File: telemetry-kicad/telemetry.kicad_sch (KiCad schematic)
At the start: 0 parts

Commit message: Changed MCU to LQFP64 footprint, added TVS and reverse polarity protection, added buck converter chip.
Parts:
- added C1, C2, C3, C4, C5, C6: 1uF, symbol Device:C
- added C10, C11: 1uF, Capacitor_SMD:C_0402_1005Metric_Pad0.74x0.62mm_HandSolder, symbol Device:C
- added C7, C8: 10uF, symbol Device:C
- added C9: 10uF, Capacitor_SMD:C_0402_1005Metric_Pad0.74x0.62mm_HandSolder, symbol Device:C
- added D1: BZT52-C15S-AU_R1_000A1, symbol Device:D_Zener
- added D2: D20V0L1B2LP-7B, symbol Device:D_TVS
- added F1: 100mA Polyfuse, Capacitor_SMD:C_0603_1608Metric_Pad1.08x0.95mm_HandSolder, symbol Device:Polyfuse
- added Q1: DMP3099LQ-7, Package_TO_SOT_SMD:SOT-23, symbol Transistor_FET:DMP3099L
- added R1: 10k, symbol Device:R_US
- added R2: 10K, symbol Device:R_US
- added SW1: SW_NRST, symbol Switch:SW_Push
- added SW2: SW_BOOT0, symbol Switch:SW_Push
- added U1: STM32H523RCT7, LQFP64_STM, symbol telemetry:STM32H523RCT7
- added U2: AP2112K-3.3, Package_TO_SOT_SMD:SOT-23-5, symbol Regulator_Linear:AP2112K-3.3
- added U3: LMR33630ADDA, Package_SO:Texas_HSOP-8-1EP_3.9x4.9mm_P1.27mm_ThermalVias, symbol Regulator_Switching:LMR33630ADDA
- added U4: ASM330LHHXG1TR, LGA14_2P5X3_STM, symbol telemetry:ASM330LHHXG1TR
- added U5: TCAN1044VDRQ1, D0008A-IPC_A, symbol telemetry:TCAN1044VDRQ1
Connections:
- new net: R1.1, SW2.1, U1.60 (BOOT0)
- new net: C1.1, C2.1, C3.1, C4.1, C6.1, C7.1, C8.1
- new net: SW1.1, U1.7 (NRST)
- new net: U3.1 (GND), U3.9 (GND)
- new net: D1.1 (K), Q1.2 (S)
- new net: D1.2 (A), Q1.1 (G), R2.1
- new net +3.3V: C5.1, SW2.2, U1.1 (VBAT), U1.13 (VDDA), U1.19 (VDD), U1.32 (VDD), U1.48 (VDD), U1.64 (VDD)
- new net +3V3: C11.1, U2.5 (VOUT)
- new net Earth: C1.2, C2.2, C3.2, C4.2, C5.2, C6.2, C7.2, C8.2, D2.2 (A2), R1.2, R2.2, SW1.2, U1.12 (VSSA), U1.18 (VSS), U1.31 (VSS), U1.47 (VSS), U1.63 (VSS)
- new net GND: C10.2, C11.2, C9.1, U2.2 (GND)
- new net VBUS: F1.1
- new net VIN: D2.1 (A1), Q1.3 (D)
- new net VIN_LDO: C10.1, C9.2, F1.2, U2.1 (VIN), U2.3 (EN)
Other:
- note added: "Linear Voltage Regulator"
- note added: "Reverse Polarity Protection and TVS"

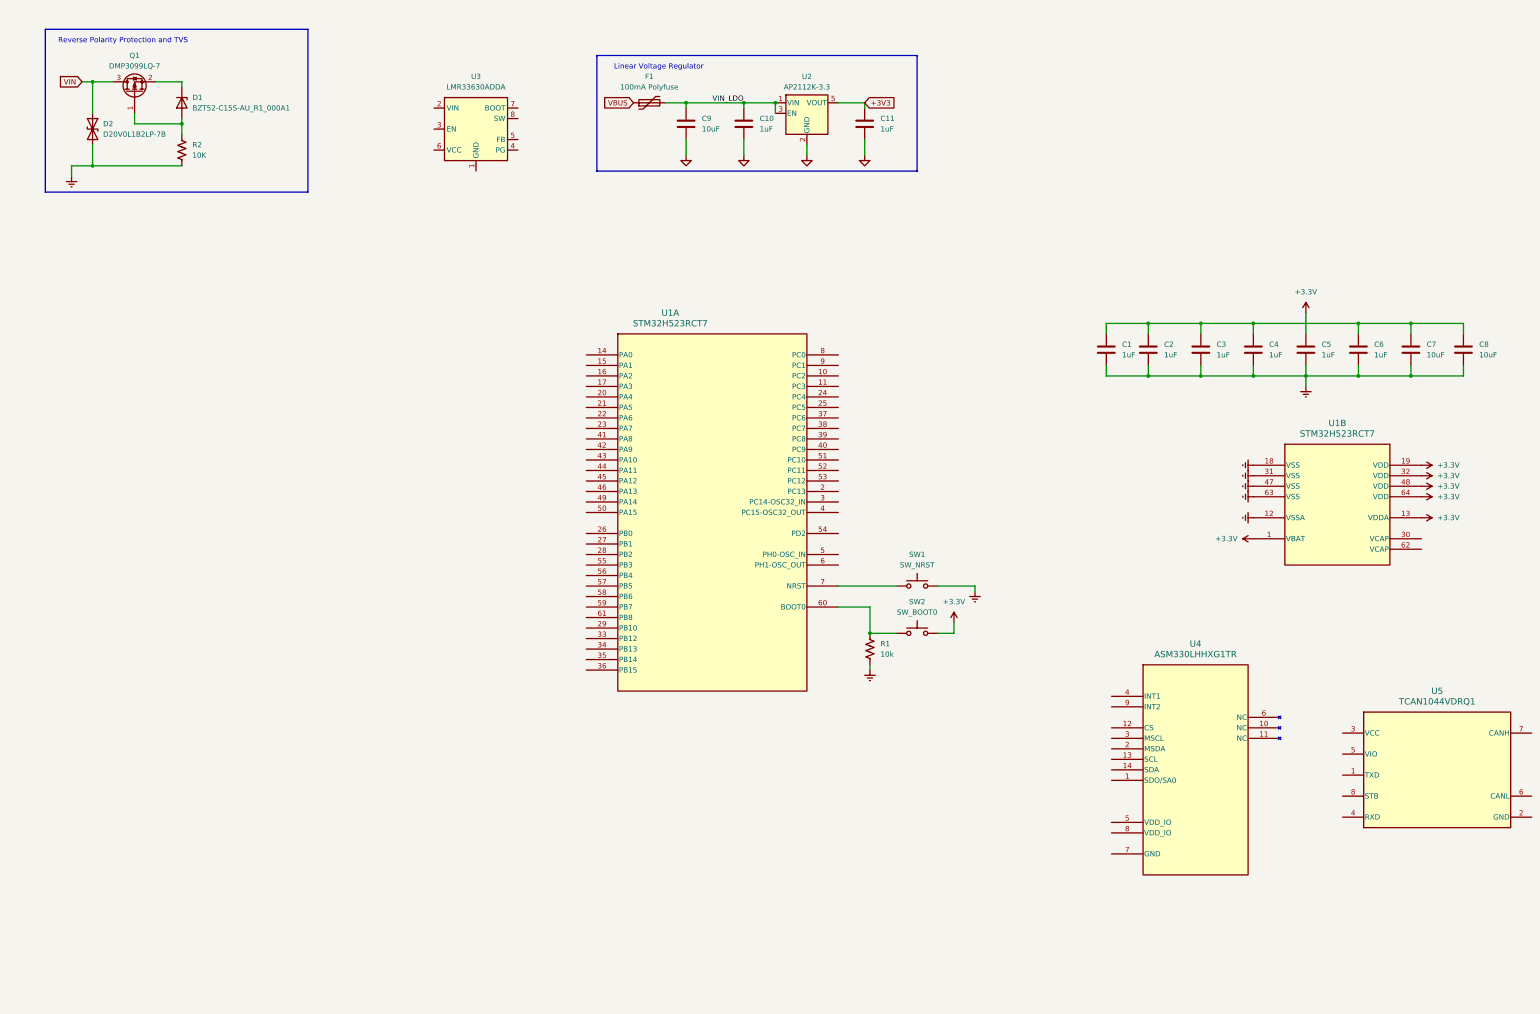
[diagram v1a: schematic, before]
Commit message: Developed schematic with all components, need to check Ublox integration and STM32 USB debugging and impliment SWD.
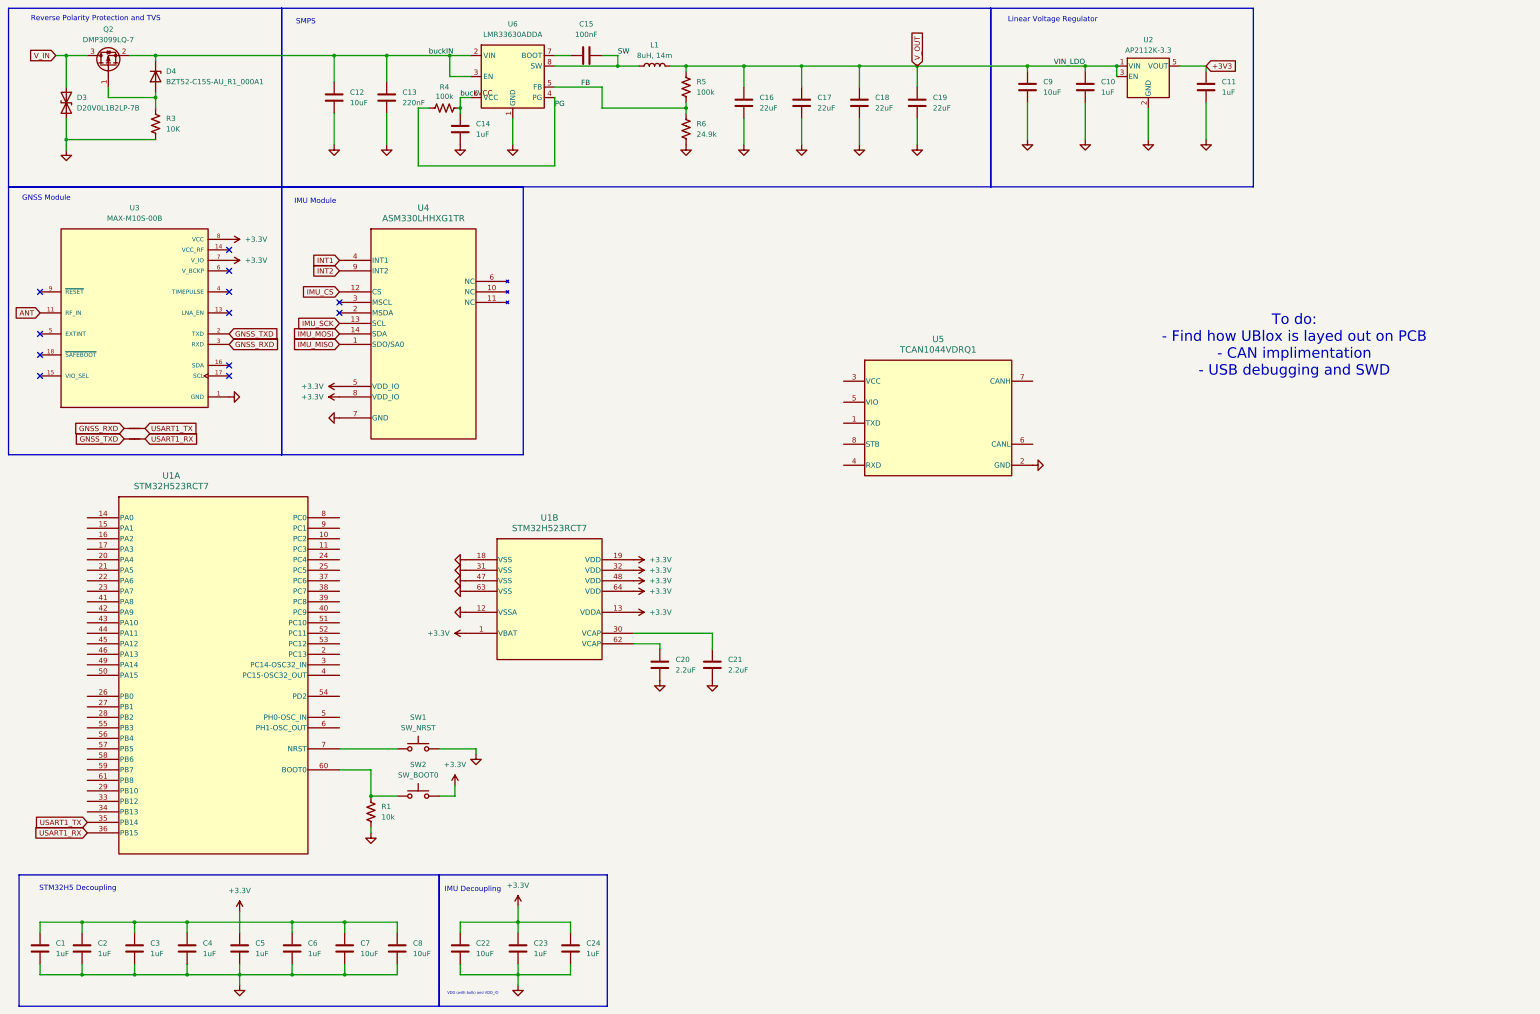
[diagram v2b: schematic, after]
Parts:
- removed D1: BZT52-C15S-AU_R1_000A1, symbol Device:D_Zener
- removed D2: D20V0L1B2LP-7B, symbol Device:D_TVS
- removed F1: 100mA Polyfuse, Capacitor_SMD:C_0603_1608Metric_Pad1.08x0.95mm_HandSolder, symbol Device:Polyfuse
- removed Q1: DMP3099LQ-7, Package_TO_SOT_SMD:SOT-23, symbol Transistor_FET:DMP3099L
- removed R2: 10K, symbol Device:R_US
- removed U3: LMR33630ADDA, Package_SO:Texas_HSOP-8-1EP_3.9x4.9mm_P1.27mm_ThermalVias, symbol Regulator_Switching:LMR33630ADDA
- added C12: 10uF, Capacitor_SMD:C_0805_2012Metric_Pad1.18x1.45mm_HandSolder, symbol Device:C
- added C13: 220nF, Capacitor_SMD:C_0805_2012Metric_Pad1.18x1.45mm_HandSolder, symbol Device:C
- added C14: 1uF, Capacitor_SMD:C_0805_2012Metric_Pad1.18x1.45mm_HandSolder, symbol Device:C
- added C15: 100nF, Capacitor_SMD:C_0805_2012Metric_Pad1.18x1.45mm_HandSolder, symbol Device:C
- added C16, C17, C18, C19: 22uF, Capacitor_SMD:C_0805_2012Metric_Pad1.18x1.45mm_HandSolder, symbol Device:C
- added C20, C21: 2.2uF, symbol Device:C
- added C22: 10uF, Capacitor_SMD:C_0402_1005Metric_Pad0.74x0.62mm_HandSolder, symbol Device:C
- added C23, C24: 1uF, Capacitor_SMD:C_0402_1005Metric_Pad0.74x0.62mm_HandSolder, symbol Device:C
- added D3: D20V0L1B2LP-7B, Capacitor_SMD:C_0402_1005Metric_Pad0.74x0.62mm_HandSolder, symbol Device:D_TVS
- added D4: BZT52-C15S-AU_R1_000A1, Diode_SMD:D_SOD-123, symbol Device:D_Zener
- added L1: 8uH, 14m, Inductor_SMD:L_TaiTech_TMPC1265_13.5x12.5mm, symbol Device:L
- added NT1, NT2: NetTie_2, symbol Device:NetTie_2
- added Q2: DMP3099LQ-7, Package_TO_SOT_SMD:SOT-23, symbol Transistor_FET:DMP3099L
- added R3: 10K, Capacitor_SMD:C_0805_2012Metric_Pad1.18x1.45mm_HandSolder, symbol Device:R_US
- added R4, R5: 100k, Capacitor_SMD:C_0805_2012Metric_Pad1.18x1.45mm_HandSolder, symbol Device:R_US
- added R6: 24.9k, Capacitor_SMD:C_0805_2012Metric_Pad1.18x1.45mm_HandSolder, symbol Device:R_US
- added U3: MAX-M10S-00B, MAX-M10S-00B, symbol telemetry:MAX-M10S-00B
- added U6: LMR33630ADDA, Package_SO:Texas_HSOP-8-1EP_3.9x4.9mm_P1.27mm_ThermalVias, symbol Regulator_Switching:LMR33630ADDA
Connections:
- net Earth is gone; now on net GND: C1.2, C2.2, C3.2, C4.2, C5.2, C6.2, C7.2, C8.2, R1.2, SW1.2, U1.12 (VSSA), U1.18 (VSS), U1.31 (VSS), U1.47 (VSS), U1.63 (VSS)
- net +3.3V: now also U4.5 (VDD_IO), U4.8 (VDD_IO), C22.2, C23.1, C24.1, U3.7 (V_IO), U3.8 (VCC)
- net GND: now also U4.7 (GND), U5.2 (GND), C12.2, C13.2, C14.2, C16.2, C17.2, C18.2, C19.2, C20.2, C21.2, C22.1, C23.2, C24.2, D3.2 (A2), R3.2, R6.2, U3.1 (GND), U3.10 (GND), U3.12 (GND), U6.1 (GND), U6.9 (GND)
- net IMU_MISO: now reaches U4.1 (SDO/SA0)
- net IMU_CS: now reaches U4.12 (CS)
- net IMU_SCK: now reaches U4.13 (SCL)
- net IMU_MOSI: now reaches U4.14 (SDA)
- net INT1: now reaches U4.4 (INT1)
- net INT2: now reaches U4.9 (INT2)
- net at U1.30 (VCAP): now also C21.1
- net at U1.62 (VCAP): now also C20.1
- net USART1_TX: now reaches U1.35 (PB14)
- net USART1_TX: now also NT2.1
- net USART1_RX: now reaches U1.36 (PB15)
- net USART1_RX: now also NT1.1
- net VIN_LDO renamed V_OUT
- net V_OUT: now also C16.1, C17.1, C18.1, C19.1, L1.2, R5.1
- new net: D4.2 (A), Q2.1 (G), R3.1
- new net: C15.1, U6.7 (BOOT)
- new net ANT: U3.11 (RF_IN)
- new net FB: R5.2, R6.1, U6.5 (FB)
- new net GNSS_RXD: NT2.2, U3.3 (RXD)
- new net GNSS_TXD: NT1.2, U3.2 (TXD)
- new net PG: R4.1, U6.4 (PG)
- new net SW: C15.2, L1.1, U6.8 (SW)
- new net V_IN: D3.1 (A1), Q2.3 (D)
- new net buckIN: C12.1, C13.1, D4.1 (K), Q2.2 (S), U6.2 (VIN), U6.3 (EN)
- new net buckVCC: C14.1, R4.2, U6.6 (VCC)
- no-connect marks 0 -> 12
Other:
- note added: "GNSS Module"
- note added: "IMU Decoupling"
- note added: "IMU Module"
- note added: "SMPS"
- note added: "STM32H5 Decoupling"
- note added: "To do: - Find how UBlox is layed out on PCB - CAN implimentation - USB debugging and SWD"
- note added: "VDD (with bulk) and VDD_IO"
- moved on the sheet: C1, C10, C11, C2, C3, C4, C5, C6, C7, C8, C9, R1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

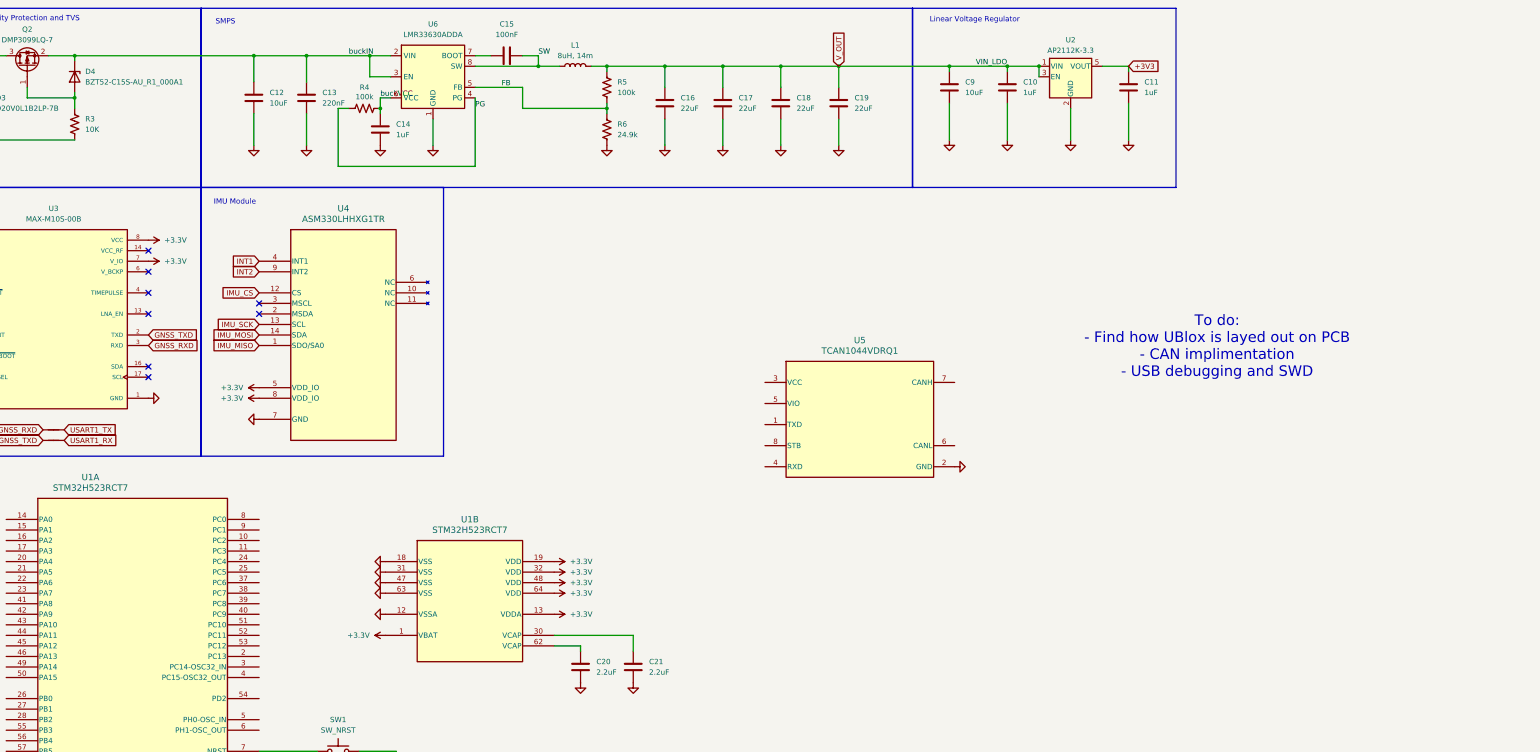
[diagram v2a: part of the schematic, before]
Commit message: Added power mux between USB and 12V car power
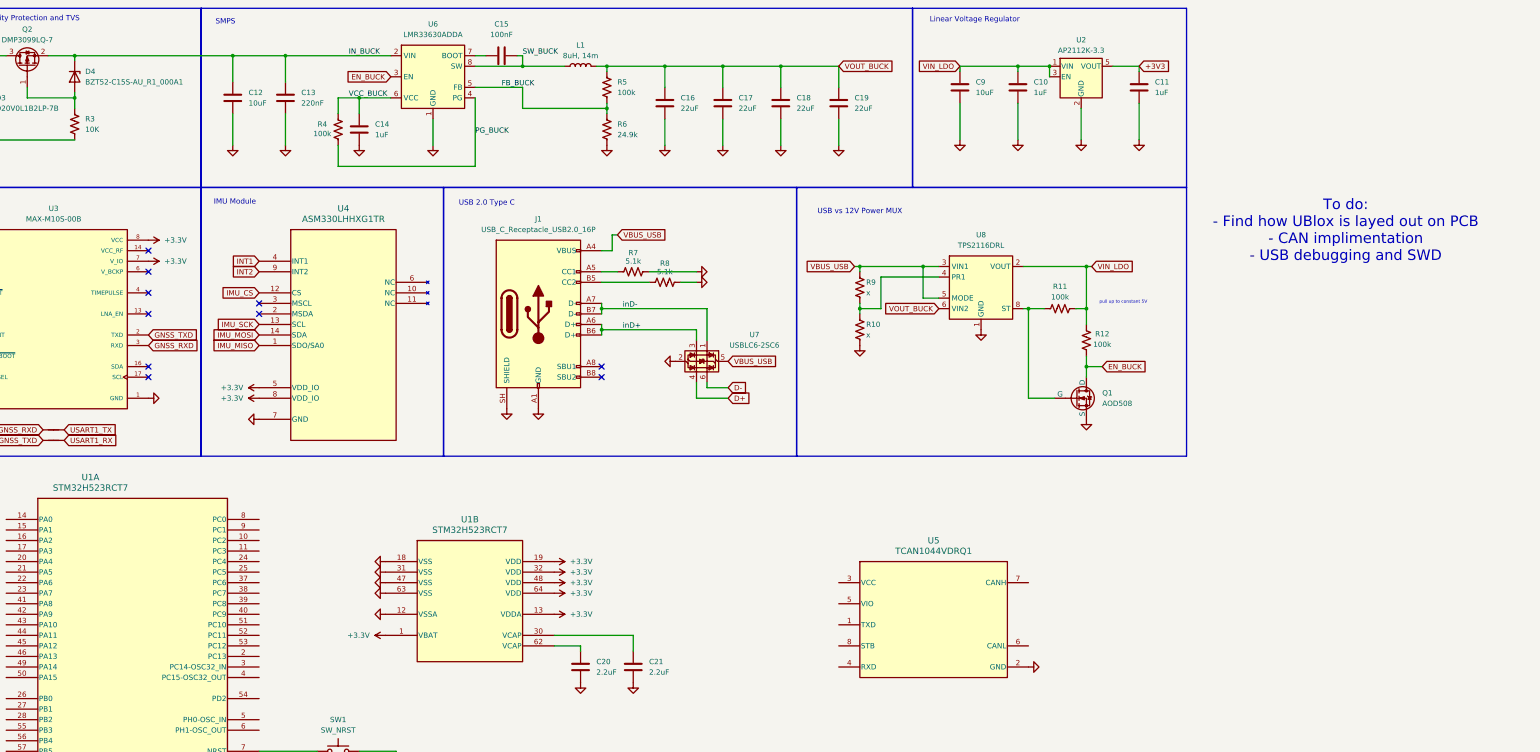
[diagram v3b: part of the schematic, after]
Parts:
- added J1: USB_C_Receptacle_USB2.0_16P, symbol Connector:USB_C_Receptacle_USB2.0_16P
- added Q1: AOD508, Package_TO_SOT_SMD:TO-252-3_TabPin4, symbol Simulation_SPICE:NMOS
- added R10, R9: x, Capacitor_SMD:C_0805_2012Metric_Pad1.18x1.45mm_HandSolder, symbol Device:R_US
- added R11, R12: 100k, Capacitor_SMD:C_0805_2012Metric_Pad1.18x1.45mm_HandSolder, symbol Device:R_US
- added R7, R8: 5.1k, Capacitor_SMD:C_0805_2012Metric_Pad1.18x1.45mm_HandSolder, symbol Device:R_US
- added U7: USBLC6-2SC6, Package_TO_SOT_SMD:SOT-23-6, symbol Power_Protection:USBLC6-2SC6
- added U8: TPS2116DRL, Package_TO_SOT_SMD:SOT-583-8, symbol Power_Management:TPS2116DRL
- U1: footprint LQFP64_STM -> (none)
- U3: footprint MAX-M10S-00B -> (none)
- U4: footprint LGA14_2P5X3_STM -> (none)
- U5: footprint D0008A-IPC_A -> (none)
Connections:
- net GND: now also J1.A1 (GND), J1.A12 (GND), J1.B1 (GND), J1.B12 (GND), J1.SH (SHIELD), Q1.3 (S), R10.2, R7.2, R8.2, U7.2 (GND), U8.1 (GND)
- net FB renamed FB_BUCK
- net PG renamed PG_BUCK
- net SW renamed SW_BUCK
- net V_OUT renamed VOUT_BUCK
- net VOUT_BUCK: now also U8.6 (VIN2); no longer C10.1, C9.2, U2.1 (VIN), U2.3 (EN)
- net buckIN renamed IN_BUCK
- net IN_BUCK: no longer U6.3 (EN)
- net buckVCC renamed VCC_BUCK
- new net: Q1.2 (G), R11.2, U8.8 (ST)
- new net: R10.1, R9.2, U8.4 (PR1)
- new net: J1.A5 (CC1), R7.1
- new net: J1.B5 (CC2), R8.1
- new net D+: U7.4 (I/O2)
- new net D-: U7.6 (I/O1)
- new net EN_BUCK: Q1.1 (D), R12.1, U6.3 (EN)
- new net VBUS_USB: J1.A4 (VBUS), J1.A9 (VBUS), J1.B4 (VBUS), J1.B9 (VBUS), R9.1, U7.5 (VBUS), U8.3 (VIN1), U8.5 (MODE)
- new net VIN_LDO: C10.1, C9.2, R11.1, R12.2, U2.1 (VIN), U2.3 (EN), U8.2 (VOUT), U8.7 (VOUT)
- new net inD+: J1.A6 (D+), J1.B6 (D+), U7.3 (I/O2)
- new net inD-: J1.A7 (D-), J1.B7 (D-), U7.1 (I/O1)
- no-connect marks 12 -> 14
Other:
- note added: "USB 2.0 Type C"
- note added: "USB vs 12V Power MUX"
- note added: "pull up to constant 5V"
- moved on the sheet: C10, C11, C12, C13, C14, C15, C9, L1, U2, U5

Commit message: Removed power mux status being used to switch off buck, the buck has a tiny quiessant current which is acceptable
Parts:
- removed Q1: AOD508, Package_TO_SOT_SMD:TO-252-3_TabPin4, symbol Simulation_SPICE:NMOS
- removed R11, R12: 100k, Capacitor_SMD:C_0805_2012Metric_Pad1.18x1.45mm_HandSolder, symbol Device:R_US
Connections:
- net EN_BUCK is gone; now on net IN_BUCK: U6.3 (EN)
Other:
- note removed: "pull up to constant 5V"
- moved on the sheet: R10, R9, U8
